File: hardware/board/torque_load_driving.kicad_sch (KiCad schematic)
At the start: 32 parts, among them J4 Conn_01x02_Female, Q2 Si7336ADP, U1 ADS7049, U10 AD8615, U11 INA180A4, U12 AD8615, U17 LTC2641

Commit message: draft v0.1 pcb
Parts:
- removed C26: 10uF, Capacitor_SMD:C_0805_2012Metric, symbol Device:C
- removed C27: 100nF, Capacitor_SMD:C_0402_1005Metric, symbol Device:C
- added C27 (x2): 100nF, Capacitor_SMD:C_0402_1005Metric, symbol Device:C
- D6: value 1N4007 -> 1N4007FL; Link https://www.digikey.com/en/products/detail/smc-diode-solutions/1N4007FL/11657827? -> https://www.digikey.com/en/products/detail/smc-diode-solutions/1N4007FL/11657817
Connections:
- net GND: now also C27.1, C27.1
- net VREF_1V65: now also C27.2, C27.2
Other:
- note added: "ADS7049 Bypass Caps"
- note added: "LTC2641 Bypass Caps"
- note removed: "ADS7049 Bypass Cap"
- note removed: "Gate Driver Bypass Caps"
- note removed: "LTC2641 Bypass Cap"
- moved on the sheet: C26, C27

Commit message: update board for v0.2.0
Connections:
- net VREF_1V65 renamed VREF_3V3
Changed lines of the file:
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@@
     (effects (font (size 1.27 1.27)) (justify left bottom))
-  )
-  (global_label "VREF_1V65" (shape input) (at 95.25 71.12 0) (fields_autoplaced)
-    (effects (font (size 1.27 1.27)) (justify left))
-    (property "Intersheetrefs" "${INTERSHEET_REFS}" (at 108.5161 71.12 0)
-      (effects (font (size 1.27 1.27)) (justify left) hide)
-    )
   )
   (global_label "5V2" (shape input) (at 158.115 114.935 0) (fields_autoplaced)
@@
     )
   )
-  (global_label "VREF_1V65" (shape input) (at 81.28 172.085 0) (fields_autoplaced)
+  (global_label "VREF_3V3" (shape input) (at 130.81 108.585 0) (fields_autoplaced)
     (effects (font (size 1.27 1.27)) (justify left))
-    (property "Intersheetrefs" "${INTERSHEET_REFS}" (at 94.5461 172.085 0)
+    (property "Intersheetrefs" "${INTERSHEET_REFS}" (at 142.8666 108.585 0)
       (effects (font (size 1.27 1.27)) (justify left) hide)
     )
   )
-  (global_label "VREF_1V65" (shape input) (at 132.715 172.085 0) (fields_autoplaced)
+  (global_label "VREF_3V3" (shape input) (at 95.25 71.12 0) (fields_autoplaced)
     (effects (font (size 1.27 1.27)) (justify left))
-    (property "Intersheetrefs" "${INTERSHEET_REFS}" (at 145.9811 172.085 0)
+    (property "Intersheetrefs" "${INTERSHEET_REFS}" (at 107.3066 71.12 0)
       (effects (font (size 1.27 1.27)) (justify left) hide)
     )
@@
     )
   )
-  (global_label "VREF_1V65" (shape input) (at 130.81 108.585 0) (fields_autoplaced)
+  (global_label "VREF_3V3" (shape input) (at 81.28 172.085 0) (fields_autoplaced)
     (effects (font (size 1.27 1.27)) (justify left))
-    (property "Intersheetrefs" "${INTERSHEET_REFS}" (at 144.0761 108.585 0)
+    (property "Intersheetrefs" "${INTERSHEET_REFS}" (at 93.3366 172.085 0)
       (effects (font (size 1.27 1.27)) (justify left) hide)
     )
+  )
+  (global_label "VREF_3V3" (shape input) (at 132.715 172.085 0) (fields_autoplaced)
+    (effects (font (size 1.27 1.27)) (justify left))
+    (property "Intersheetrefs" "${INTERSHEET_REFS}" (at 144.7716 172.085 0)
+      (effects (font (size 1.27 1.27)) (justify left) hide)
+    )

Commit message: update pcb to v0.2.0
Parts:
- TP1: footprint kicad_component_library:TestPoint_Keystone_5027_Miniature -> TestPoint:TestPoint_THTPad_D3.0mm_Drill1.5mm; Link https://www.digikey.com/en/products/detail/keystone-electro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 -> n/a; Manufacturer Keystone Electronics -> n/a; Manufacturer Number 5027 -> n/a; Notes SMT testpoint with hole for added sturdiness. -> (none)
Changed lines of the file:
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@@
       (effects (font (size 1.27 1.27)) (justify left) hide)
     )
-    (property "Footprint" "kicad_component_library:TestPoint_Keystone_5027_Miniature" (at 114.935 65.405 0)
+    (property "Footprint" "TestPoint:TestPoint_THTPad_D3.0mm_Drill1.5mm" (at 114.935 65.405 0)
       (effects (font (size 1.27 1.27)) hide)
     )
-    (property "Datasheet" "https://www.keyelco.com/userAssets/file/M65p55.pdf" (at 114.935 65.405 0)
+    (property "Datasheet" "n/a" (at 114.935 65.405 0)
       (effects (font (size 1.27 1.27)) hide)
     )
-    (property "Link" "https://www.digikey.com/en/products/detail/keystone-electronics/5027/5118871" (at 120.015 65.405 0)
+    (property "Link" "n/a" (at 120.015 65.405 0)
       (effects (font (size 1.27 1.27)) hide)
     )
-    (property "Notes" "SMT testpoint with hole for added sturdiness." (at 120.015 65.405 0)
+    (property "Notes" "" (at 120.015 65.405 0)
       (effects (font (size 1.27 1.27)) hide)
     )
-    (property "Manufacturer" "Keystone Electronics" (at 120.015 65.405 0)
+    (property "Manufacturer" "n/a" (at 120.015 65.405 0)
       (effects (font (size 1.27 1.27)) hide)
     )
-    (property "Manufacturer Number" "5027" (at 120.015 65.405 0)
+    (property "Manufacturer Number" "n/a" (at 120.015 65.405 0)
       (effects (font (size 1.27 1.27)) hide)
     )

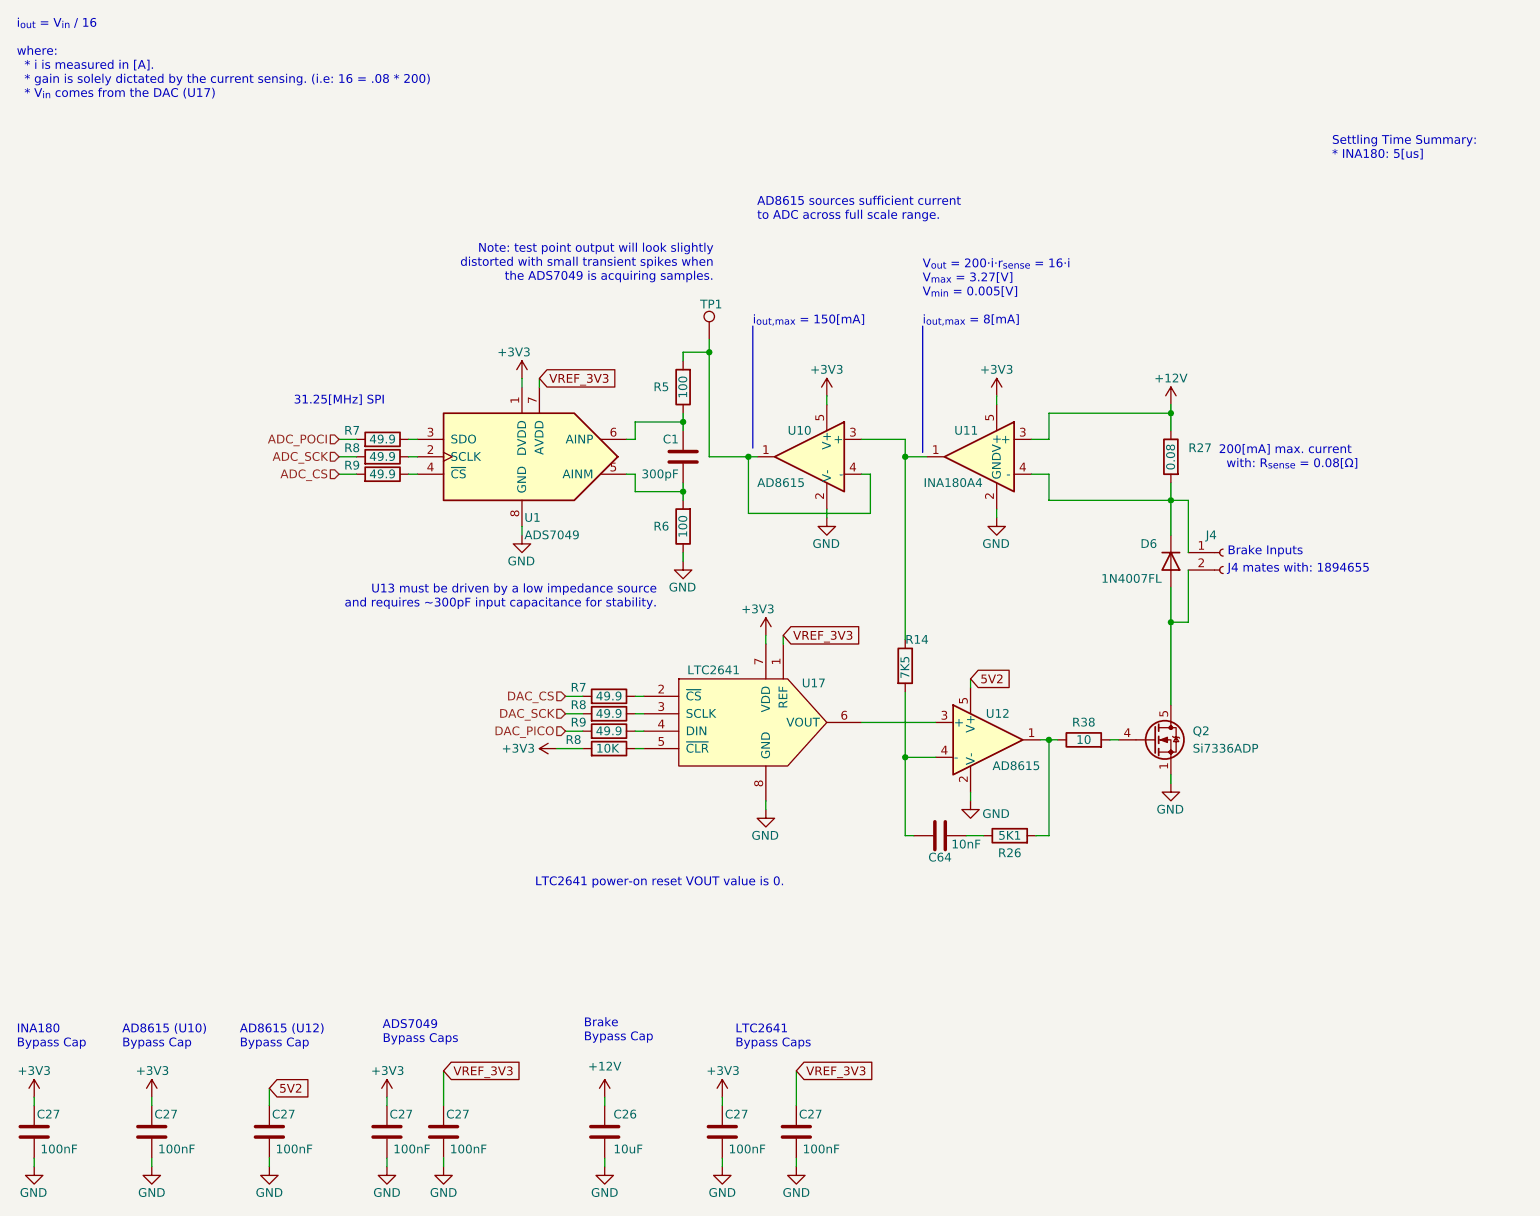
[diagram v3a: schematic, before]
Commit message: update silkscreen size; add mating connector note
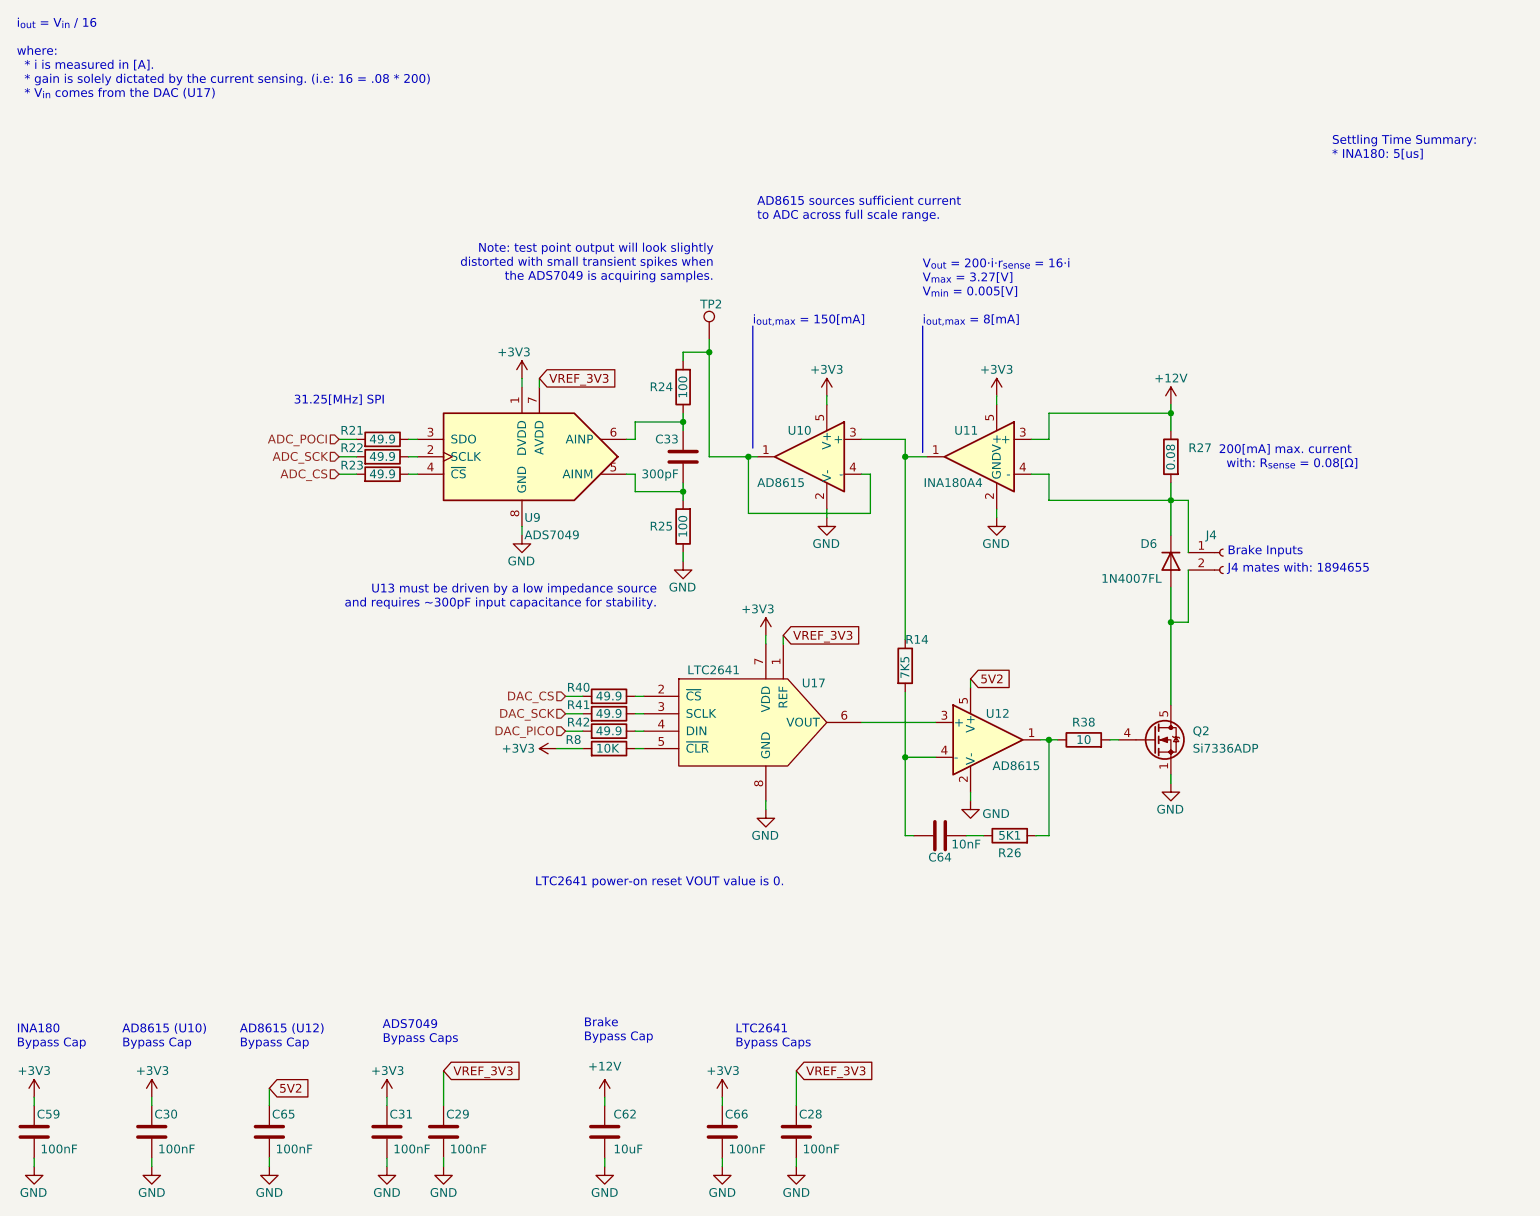
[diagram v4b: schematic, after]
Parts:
- renumbered C27 to C28, C27 to C29, C27 to C30, C27 to C31, C1 to C33, C27 to C59, C26 to C62, C27 to C65, C27 to C66, R7 to R21, R8 to R22, R9 to R23, R5 to R24, R6 to R25, R7 to R40, R8 to R41, R9 to R42, TP1 to TP2, U1 to U9
